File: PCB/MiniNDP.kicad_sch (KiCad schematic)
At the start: 20 parts, among them J1 Conn_02x20_Odd_Even, U1 HC161, U2 HC161, U3 HC161, U4 HC138, U5 HC574, U6 AS6C4008, U7 1G32, U8 1G79

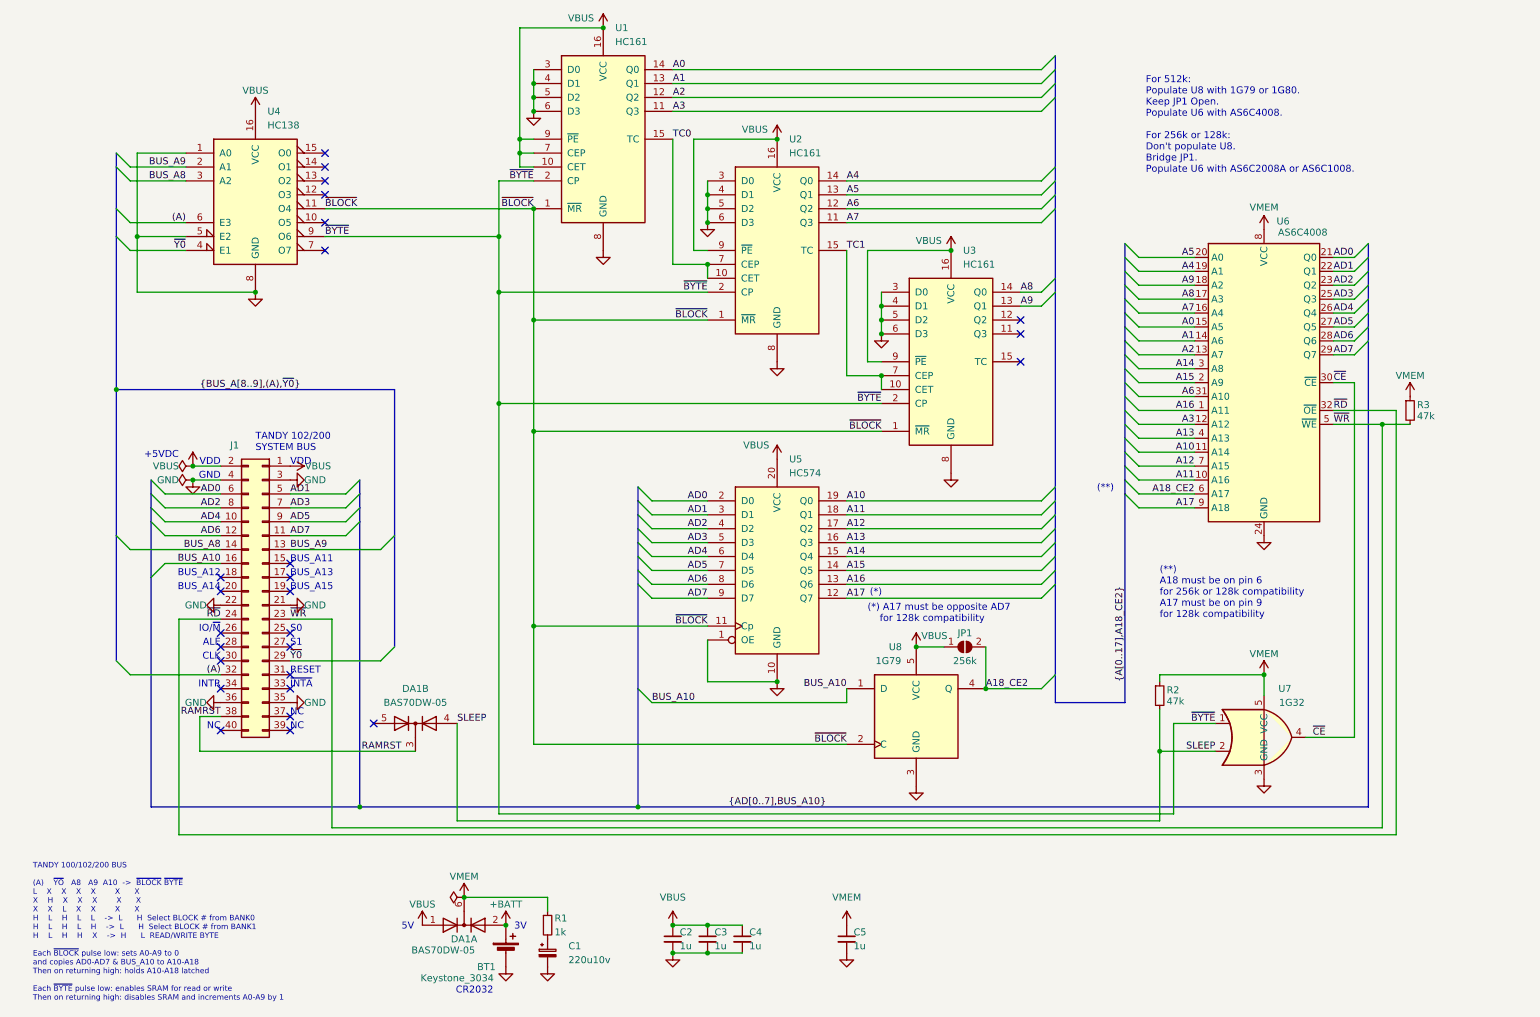
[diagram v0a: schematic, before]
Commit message: make E version default, easier to solder
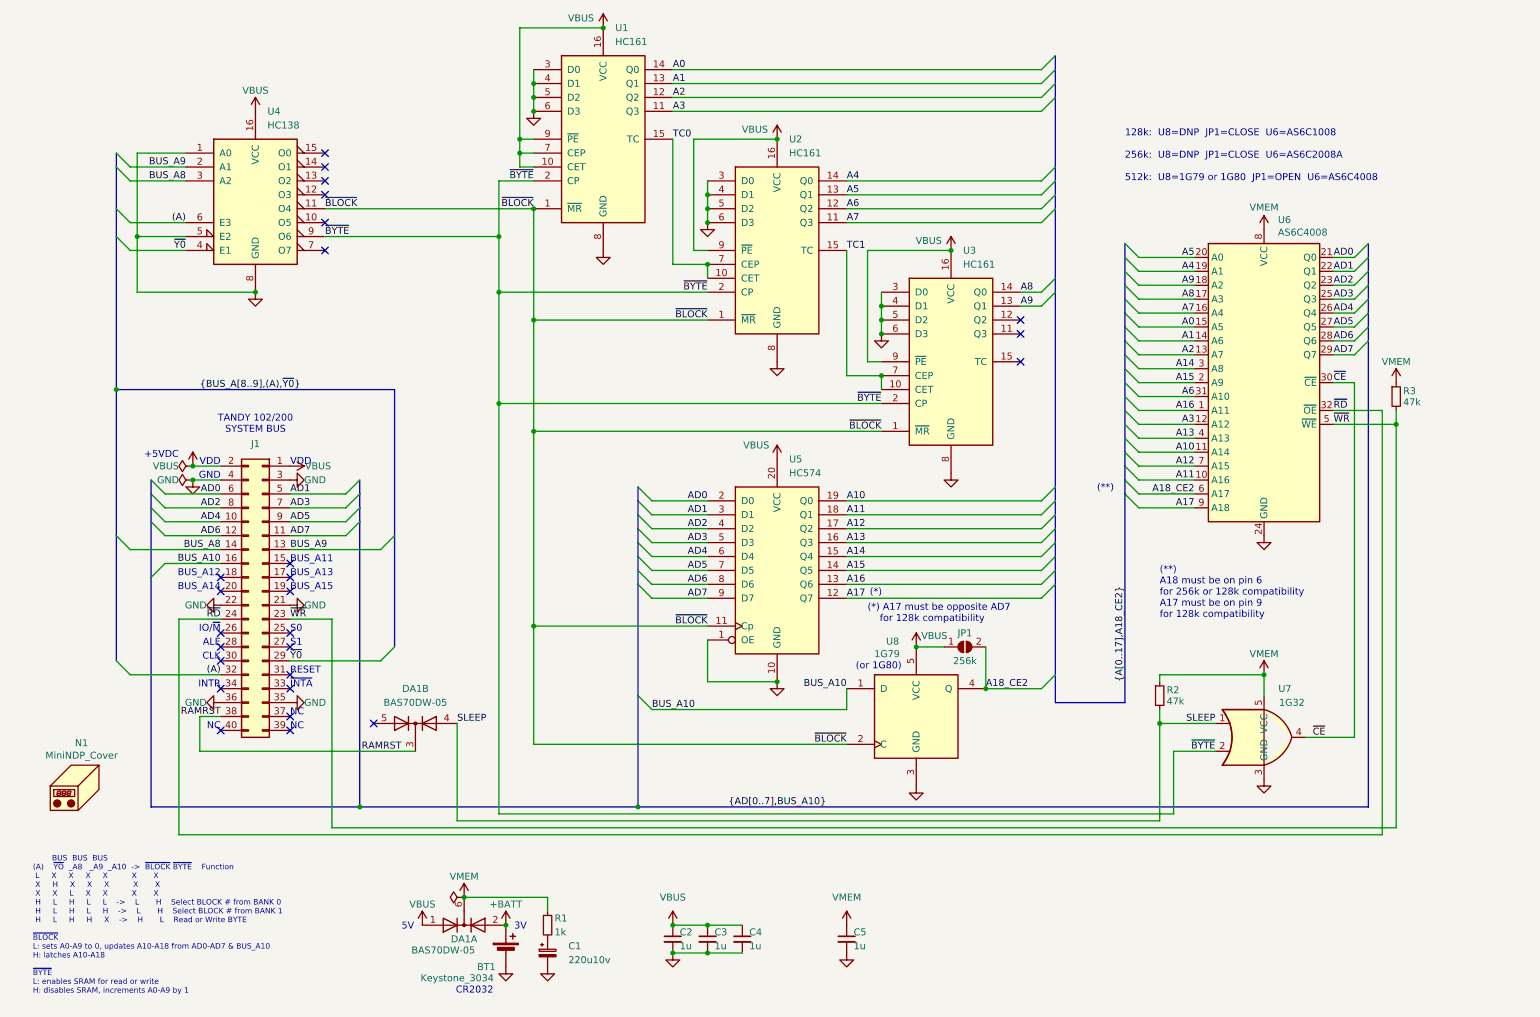
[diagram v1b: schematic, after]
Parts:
- added N1: MiniNDP_Cover, 000_LOCAL:MiniNDP_Cover, symbol 000_LOCAL:Housing
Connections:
- net SLEEP: now also U7.1; no longer U7.2
- net ~{BYTE}: now also U7.2; no longer U7.1
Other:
- note added: "(or 1G80)"
- note added: "128k: U8=DNP JP1=CLOSE U6=AS6C1008 256k: U8=DNP JP1=CLOSE U6=AS6C2008A 512k: U8=1G79 or 1G80 JP1=OPEN U6=AS6C4008"
- note added: "BUS BUS BUS (A) ~{YO} _A8 _A9 _A10 -> ~{BLOCK} ~{BYTE} Function L X X X X X X X H X X X X X X X L X X X X H L H L L -> L H Select BLOCK # from BANK 0 H L H L H -> L H Select BLOCK # from BANK 1 H L H H X -> H L Read or Write BYTE ~{BLOCK} L: sets A0-A9 to 0, updates A10-A18 from AD0-AD7 & BUS_A10 H: latches A10-A18 ~{BYTE} L: enables SRAM for read or write H: disables SRAM, increments A0-A9 by 1"
- note removed: "For 512k: Populate U8 with 1G79 or 1G80. Keep JP1 Open. Populate U6 with AS6C4008. For 256k or 128k: Don't populate U8. Bridge JP1. Populate U6 with AS6C2008A or AS6C1008."
- note removed: "TANDY 100/102/200 BUS (A) ~{YO} A8 A9 A10 -> ~{BLOCK} ~{BYTE} L X X X X X X X H X X X X X X X L X X X X H L H L L -> L H Select BLOCK # from BANK0 H L H L H -> L H Select BLOCK # from BANK1 H L H H X -> H L READ/WRITE BYTE Each ~{BLOCK} pulse low: sets A0-A9 to 0 and copies AD0-AD7 & BUS_A10 to A10-A18 Then on returning high: holds A10-A18 latched Each ~{BYTE} pulse low: enables SRAM for read or 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"
- title: MiniNDP 512 -> MiniNDP
- moved on the sheet: R3
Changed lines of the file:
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@@
 	(paper "A4")
 	(title_block
-		(title "MiniNDP 512")
-		(date "2024-11-13")
-		(rev "E03")
+		(title "MiniNDP")
+		(date "2024-11-17")
+		(rev "E04")
 		(company "Brian K. White - b.kenyon.w@gmail.com")
 		(comment 1 "github.com/bkw777/NODE_DATAPAC")
@@
 	)
 	(junction
-		(at 222.25 148.59)
-		(diameter 0)
-		(color 0 0 0 0)
-	)
-	(junction
 		(at 171.45 67.31)
 		(diameter 0)
@@
 	)
 	(junction
-		(at 262.89 88.9)
-		(diameter 0)
-		(color 0 0 0 0)
-	)
-	(junction
 		(at 105.41 36.83)
 		(diameter 0)
@@
 	)
 	(junction
+		(at 265.43 88.9)
+		(diameter 0)
+		(color 0 0 0 0)
+	)
+	(junction
 		(at 101.6 64.77)
 		(diameter 0)
@@
 	)
 	(junction
+		(at 222.25 143.51)
+		(diameter 0)
+		(color 0 0 0 0)
+	)
+	(junction
 		(at 107.95 26.67)
 		(diameter 0)
@@
 	)
 	(bus_entry
-		(at 127 137.16)
+		(at 127 138.43)
 		(size 2.54 2.54)
 		(stroke
@@
 	(wire
 		(pts
+			(xy 265.43 86.36) (xy 265.43 88.9)
+		)
+		(stroke
+			(width 0)
+			(type default)
+		)
+	)
+	(wire
+		(pts
+			(xy 222.25 143.51) (xy 222.25 161.29)
+		)
+		(stroke
+			(width 0)
+			(type default)
+		)
+	)
+	(wire
+		(pts
 			(xy 171.45 69.85) (xy 171.45 67.31)
 		)
@@
 	(wire
 		(pts
-			(xy 224.79 143.51) (xy 224.79 160.02)
+			(xy 224.79 148.59) (xy 224.79 160.02)
 		)
 		(stroke
@@
 	(wire
 		(pts
-			(xy 165.1 139.7) (xy 165.1 137.16)
+			(xy 165.1 140.97) (xy 165.1 137.16)
 		)
 		(stroke
@@
 	(bus
 		(pts
-			(xy 127 118.11) (xy 127 137.16)
+			(xy 127 118.11) (xy 127 138.43)
 		)
 		(stroke
@@
 	(wire
 		(pts
-			(xy 232.41 143.51) (xy 224.79 143.51)
+			(xy 232.41 148.59) (xy 224.79 148.59)
 		)
 		(stroke
@@
 	(wire
 		(pts
-			(xy 262.89 88.9) (xy 262.89 162.56)
+			(xy 265.43 88.9) (xy 265.43 162.56)
 		)
 		(stroke
@@
 	(wire
 		(pts
-			(xy 262.89 88.9) (xy 254 88.9)
+			(xy 254 88.9) (xy 265.43 88.9)
 		)
 		(stroke
@@
 	(wire
 		(pts
-			(xy 222.25 140.97) (xy 222.25 148.59)
+			(xy 222.25 140.97) (xy 222.25 143.51)
 		)
 		(stroke
@@
 	(wire
 		(pts
-			(xy 222.25 148.59) (xy 222.25 161.29)
-		)
-		(stroke
-			(width 0)
-			(type default)
-		)
-	)
-	(wire
-		(pts
 			(xy 218.44 58.42) (xy 228.6 58.42)
 		)
@@
 	(bus
 		(pts
-			(xy 127 137.16) (xy 127 158.75)
+			(xy 127 138.43) (xy 127 158.75)
 		)
 		(stroke
@@
 	(wire
 		(pts
-			(xy 262.89 88.9) (xy 267.97 88.9)
-		)
-		(stroke
-			(width 0)
-			(type default)
-		)
-	)
-	(wire
-		(pts
 			(xy 165.1 80.01) (xy 165.1 57.15)
 		)
@@
 	(wire
 		(pts
-			(xy 222.25 148.59) (xy 232.41 148.59)
+			(xy 222.25 143.51) (xy 232.41 143.51)
 		)
 		(stroke
@@
 	(wire
 		(pts
-			(xy 262.89 162.56) (xy 71.12 162.56)
+			(xy 265.43 162.56) (xy 71.12 162.56)
 		)
 		(stroke
@@
 	(wire
 		(pts
-			(xy 129.54 139.7) (xy 165.1 139.7)
+			(xy 129.54 140.97) (xy 165.1 140.97)
 		)
 		(stroke
@@
 	(wire
 		(pts
-			(xy 254 86.36) (xy 265.43 86.36)
+			(xy 254 86.36) (xy 262.89 86.36)
 		)
 		(stroke
@@
 	(wire
 		(pts
-			(xy 265.43 163.83) (xy 265.43 86.36)
+			(xy 262.89 163.83) (xy 262.89 86.36)
 		)
 		(stroke
@@
 	(wire
 		(pts
-			(xy 43.18 163.83) (xy 265.43 163.83)
+			(xy 43.18 163.83) (xy 262.89 163.83)
 		)
 		(stroke
@@
 	(text "TANDY 102/200\nSYSTEM BUS"
 		(exclude_from_sim no)
-		(at 57.15 93.98 0)
+		(at 57.15 88.9 0)
 		(effects
 			(font
 				(size 1.27 1.27)
 			)
-			(justify left bottom)
 		)
 	)
@@
 		)
 	)
-	(text "For 512k:\nPopulate U8 with 1G79 or 1G80.\nKeep JP1 Open.\nPopulate U6 with AS6C4008.\n\nFor 256k or 128k:\nDon't populate U8.\nBridge JP1.\nPopulate U6 with AS6C2008A or AS6C1008.\n"
+	(text "128k:  U8=DNP  JP1=CLOSE  U6=AS6C1008\n\n256k:  U8=DNP  JP1=CLOSE  U6=AS6C2008A\n\n512k:  U8=1G79 or 1G80  JP1=OPEN  U6=AS6C4008\n"
 		(exclude_from_sim no)
-		(at 219.71 43.18 0)
+		(at 215.9 44.704 0)
 		(effects
 			(font
@@
 		)
 	)
+	(text "(or 1G80)"
+		(exclude_from_sim no)
+		(at 170.942 133.096 0)
+		(effects
+			(font
+				(size 1.27 1.27)
+			)
+		)
+	)
 	(text "VDD"
 		(exclude_from_sim no)
@@
 		)
 	)
-	(text "TANDY 100/102/200 BUS\n\n(A)	~{YO}   A8   A9  A10  ->  ~{BLOCK} ~{BYTE}\nL	X	X	X	X		X	  X\nX	H	X	X	X		X	  X\nX	X	L	X	X		X	  X\nH	L	H	L	L	->  L	  H  Select BLOCK # from BANK0\nH	L	H	L	H	->  L	  H  Select BLOCK # from BANK1\nH	L	H	H	X	->  H	  L  READ/WRITE BYTE\n\nEach ~{BLOCK} pulse low: sets A0-A9 to 0\nand copies AD0-AD7 & BUS_A10 to A10-A18\nThen on returning high: holds A10-A18 latched\n\nEach ~{BYTE} pulse low: enables SRAM for read or write\nThen on returning high: disables SRAM and increments A0-A9 by 1\n"
+	(text "	    BUS  BUS  BUS\n(A)	~{YO}  _A8   _A9  _A10  ->  ~{BLOCK} ~{BYTE}    Function\n L	 X	 X	 X	 X		  X	   X\n X	 H	 X	 X	 X		  X	   X\n X	 X	 L	 X	 X		  X	   X\n H	 L	 H	 L	 L	->    L	   H	Select BLOCK # from BANK 0\n H	 L	 H	 L	 H	->    L	   H	Select BLOCK # from BANK 1\n H	 L	 H	 H	 X	->    H	   L	Read or Write BYTE\n\n~{BLOCK}\nL: sets A0-A9 to 0, updates A10-A18 from AD0-AD7 & BUS_A10\nH: latches A10-A18\n\n~{BYTE}\nL: enables SRAM for read or write\nH: disables SRAM, increments A0-A9 by 1\n"
 		(exclude_from_sim no)
-		(at 16.51 194.31 0)
+		(at 16.51 193.04 0)
 		(effects
 			(font
@@
 	)
 	(label "BUS_A10"
-		(at 129.54 139.7 0)
+		(at 129.54 140.97 0)
 		(fields_autoplaced yes)
 		(effects
@@
 	)
 	(label "SLEEP"
-		(at 232.41 148.59 180)
+		(at 232.41 143.51 180)
 		(fields_autoplaced yes)
 		(effects
@@
 	)
 	(label "~{BYTE}"
-		(at 232.41 143.51 180)
+		(at 232.41 148.59 180)
 		(fields_autoplaced yes)
 		(effects
@@
 	)
 	(symbol
+		(lib_id "000_LOCAL:Housing")
+		(at 25.4 154.94 0)
+		(unit 1)
+		(exclude_from_sim yes)
+		(in_bom no)
+		(on_board yes)
+		(dnp no)
+		(property "Reference" "N1"
+			(at 25.4 147.066 0)
+			(effects
+				(font
+					(size 1.27 1.27)
+				)
+			)
+		)
+		(property "Value" "MiniNDP_Cover"
+			(at 25.4 149.352 0)
+			(effects
+				(font
+					(size 1.27 1.27)
+				)
+			)
+		)
+		(property "Footprint" "000_LOCAL:MiniNDP_Cover"
+			(at 26.67 153.67 0)
+			(effects
+				(font
+					(size 1.27 1.27)
+				)
+				(hide yes)
+			)
+		)
+		(property "Datasheet" "../COVER/MiniNDP_Cover.scad"
+			(at 26.67 153.67 0)
+			(effects
+				(font
+					(size 1.27 1.27)
+				)
+				(hide yes)
+			)
+		)
+		(property "Description" "Snap cover for MiniNDP"
+			(at 25.4 154.94 0)
+			(effects
+				(font
+					(size 1.27 1.27)
+				)
+				(hide yes)
+			)
+		)
+		(property "MPN" "MiniNDP_Cover.stl"
+			(at 25.4 154.94 0)
+			(effects
+				(font
+					(size 1.27 1.27)
+				)
+				(hide yes)
+			)
+		)
+		(instances
+			(project ""
+				(path "/f15c2929-5cf4-4b4e-965d-148e1bec8a42"
+					(reference "N1")
+					(unit 1)
+				)
+			)
+		)
+	)
+	(symbol
 		(lib_id "000_LOCAL:AS6C4008_TSOP")
 		(at 241.3 78.74 0)
@@
 		(dnp no)
 		(property "Reference" "U6"
-			(at 243.586 51.816 0)
+			(at 243.84 51.562 0)
 			(effects
 				(font
@@
 	(symbol
 		(lib_id "000_LOCAL:R")
-		(at 267.97 86.36 0)
+		(at 265.43 83.82 0)
 		(unit 1)
 		(exclude_from_sim no)
@@
 		(dnp no)
 		(property "Reference" "R3"
-			(at 269.24 85.344 0)
+			(at 266.7 82.804 0)
 			(effects
 				(font
@@
 		)
 		(property "Value" "47k"
-			(at 269.24 87.376 0)
+			(at 266.7 84.836 0)
 			(effects
 				(font
@@
 		)
 		(property "Footprint" "000_LOCAL:R_0805"
-			(at 267.97 86.36 0)
+			(at 265.43 83.82 0)
 			(effects
 				(font
@@
 		)
 		(property "Datasheet" "datasheets/sei-rmcf_rmcp.pdf"
-			(at 267.97 86.36 0)
+			(at 265.43 83.82 0)
 			(effects
 				(font
@@
 		)
 		(property "Description" "RES 47K OHM 1% 1/8W 0805"
-			(at 267.97 86.36 0)
+			(at 265.43 83.82 0)
 			(effects
 				(font
@@
 		)
 		(property "MPN" "RMCF0805FT47K0"
-			(at 267.97 86.36 0)
+			(at 265.43 83.82 0)
 			(effects
 				(font
@@
 		(dnp no)
 		(property "Reference" "U8"
-			(at 173.99 129.54 0)
+			(at 173.482 128.524 0)
 			(effects
 				(font
@@
 		)
 		(property "Value" "1G79"
-			(at 172.72 132.08 0)
+			(at 172.466 130.81 0)
 			(effects
 				(font
@@
 	(symbol
 		(lib_id "power:VMEM")
-		(at 267.97 83.82 0)
+		(at 265.43 81.28 0)
 		(unit 1)
 		(exclude_from_sim no)
@@
 		(dnp no)
 		(property "Reference" "#PWR013"
-			(at 267.97 87.63 0)
+			(at 265.43 85.09 0)
 			(effects
 				(font
@@
 		)
 		(property "Value" "VMEM"
-			(at 267.97 80.01 0)
+			(at 265.43 77.47 0)
 			(effects
 				(font
@@
 		)
 		(property "Footprint" ""
-			(at 267.97 83.82 0)
+			(at 265.43 81.28 0)
 			(effects
 				(font
@@
 		)
 		(property "Datasheet" ""
-			(at 267.97 83.82 0)
+			(at 265.43 81.28 0)
 			(effects
 				(font
@@
 		)
 		(property "Description" ""
-			(at 267.97 83.82 0)
+			(at 265.43 81.28 0)
 			(effects
 				(font
@@
 		(dnp no)
 		(property "Reference" "J1"
-			(at 53.34 92.71 0)
+			(at 57.15 92.456 0)
 			(effects
 				(font
